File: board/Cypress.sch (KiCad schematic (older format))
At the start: 55 parts, among them J1 USB_MICRO_B, U2 CY7C68013A, X1 CRYSTAL

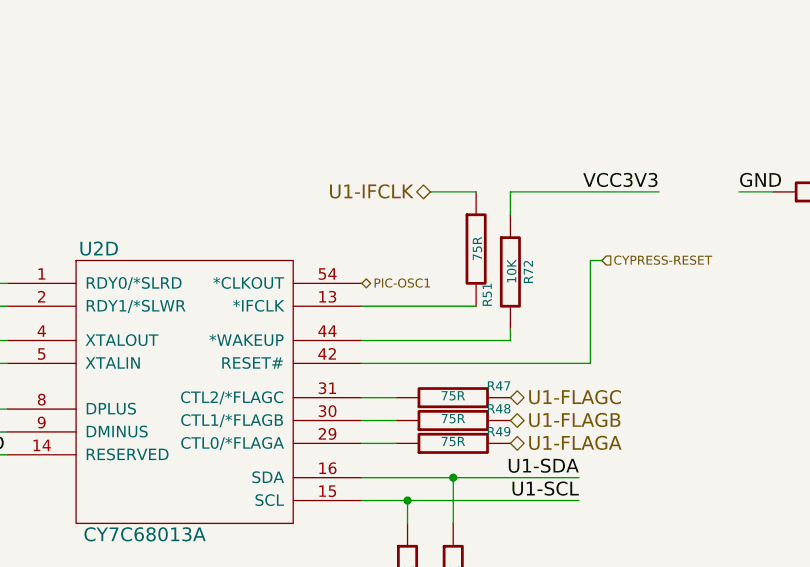
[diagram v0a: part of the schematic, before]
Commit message: Issue #1458 - HDMI RX TX pins added, Cypress added, DDR added
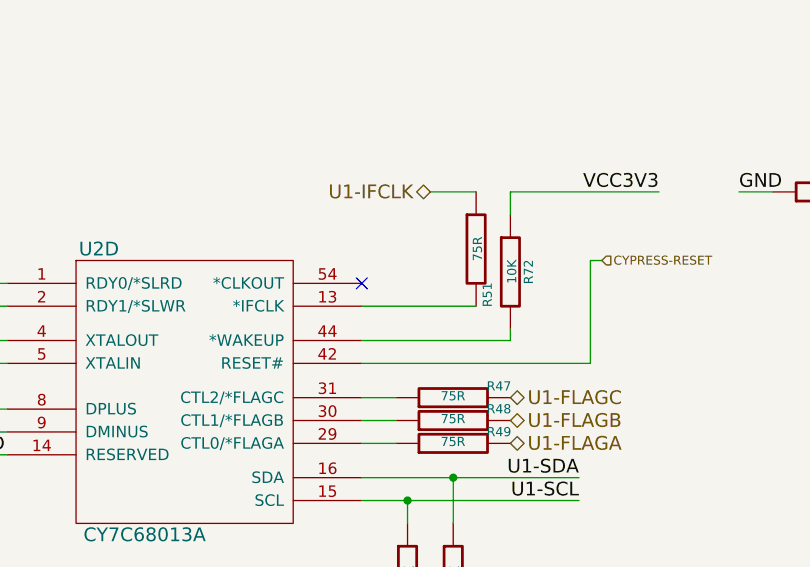
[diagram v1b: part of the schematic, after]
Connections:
- net PIC-OSC1: no longer names the net of U2.54 (*CLKOUT)
- no-connect marks 1 -> 2
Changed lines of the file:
@@
 Sheet 7 10
 Title "HDMI2USB"
-Date "11 dec 2014"
+Date "17 dec 2014"
 Rev "Rev2"
 Comp ""
@@
 Text Label 4700 1700 2    60   ~ 0
 GND
-Text HLabel 10100 3950 2    39   BiDi ~ 0
-PIC-OSC1
 $Comp
 L R R74
@@
 0D 08 60 00 00 34 20 80 01 00 D0 80 00 06 00 40 03 02 18 00 00 0D 08 60 00 00 34 20 80 01 00 D0
 80 00 06 00 40 03 02 18 00 00 0D FE 0D 6E A0 C3 78 63 AE 4C 0B 00 00 00 00 49 45 4E 44 AE 42 60
-82 03 $EndBitmap
+82 02 $EndBitmap
 EndData
 $EndBitmap
@@
 	12550 3300 12550 3550
 Connection ~ 12550 3550
+NoConn ~ 10100 3950
 $EndSCHEMATC
